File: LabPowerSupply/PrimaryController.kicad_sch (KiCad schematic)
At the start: 25 parts, among them Y1 8M

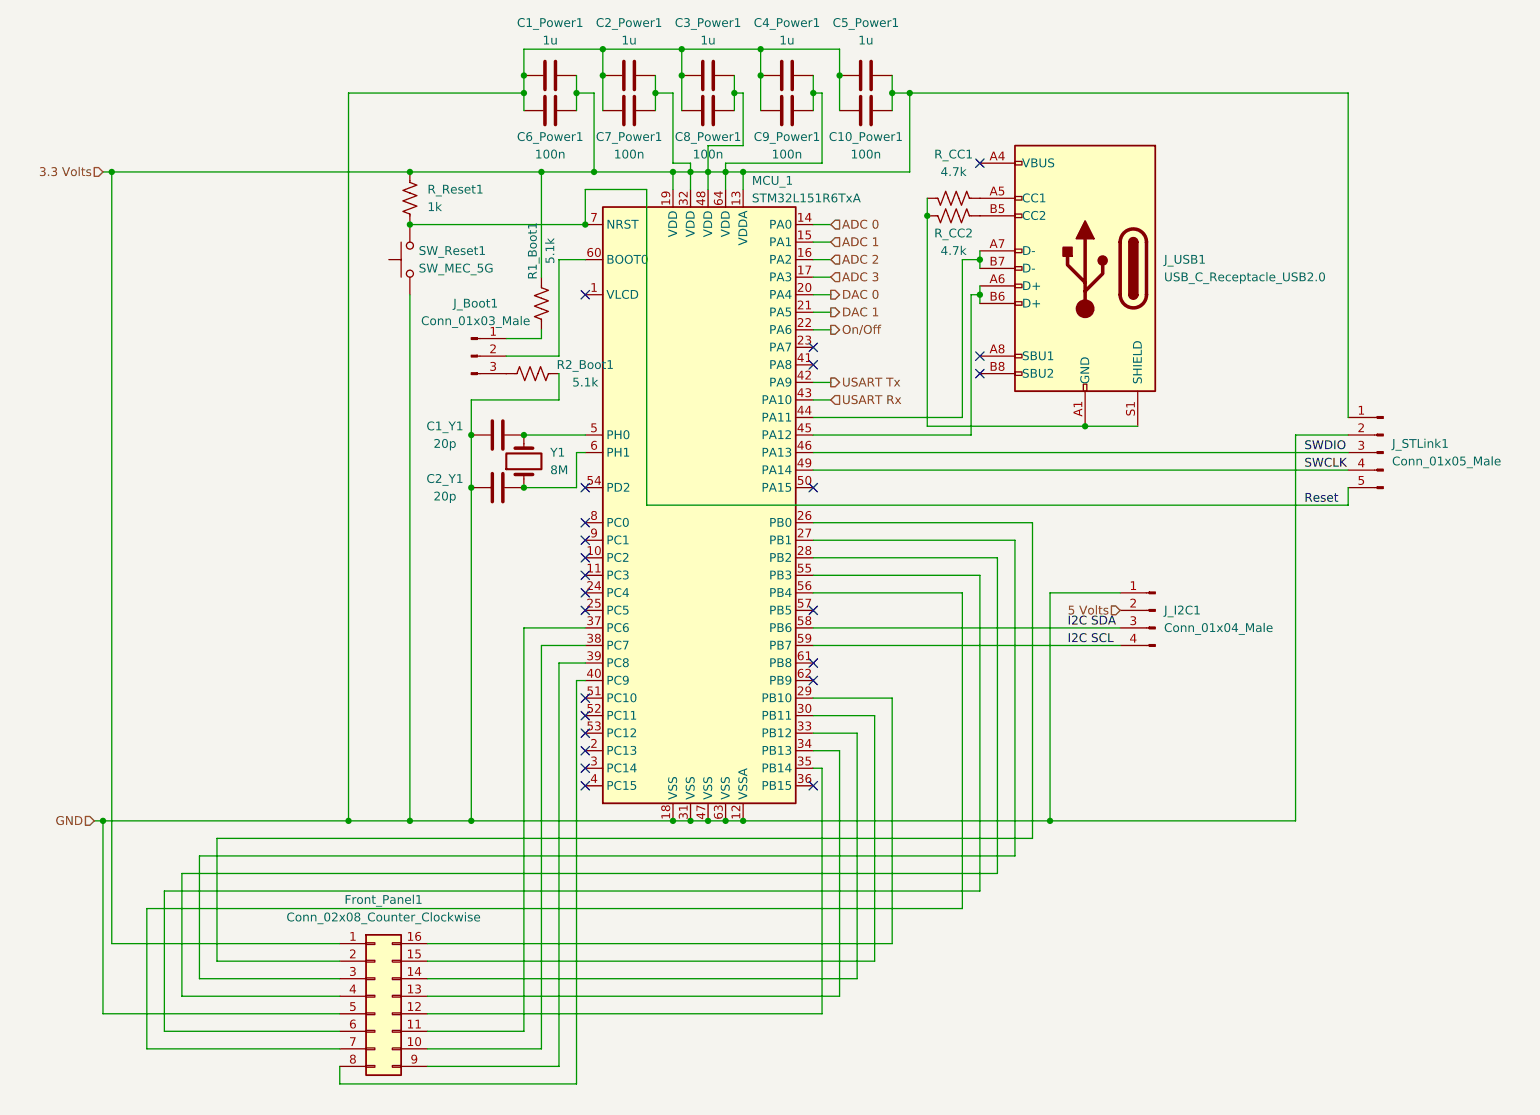
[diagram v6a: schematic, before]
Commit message: Fixed MCU communication pins and optocoupler
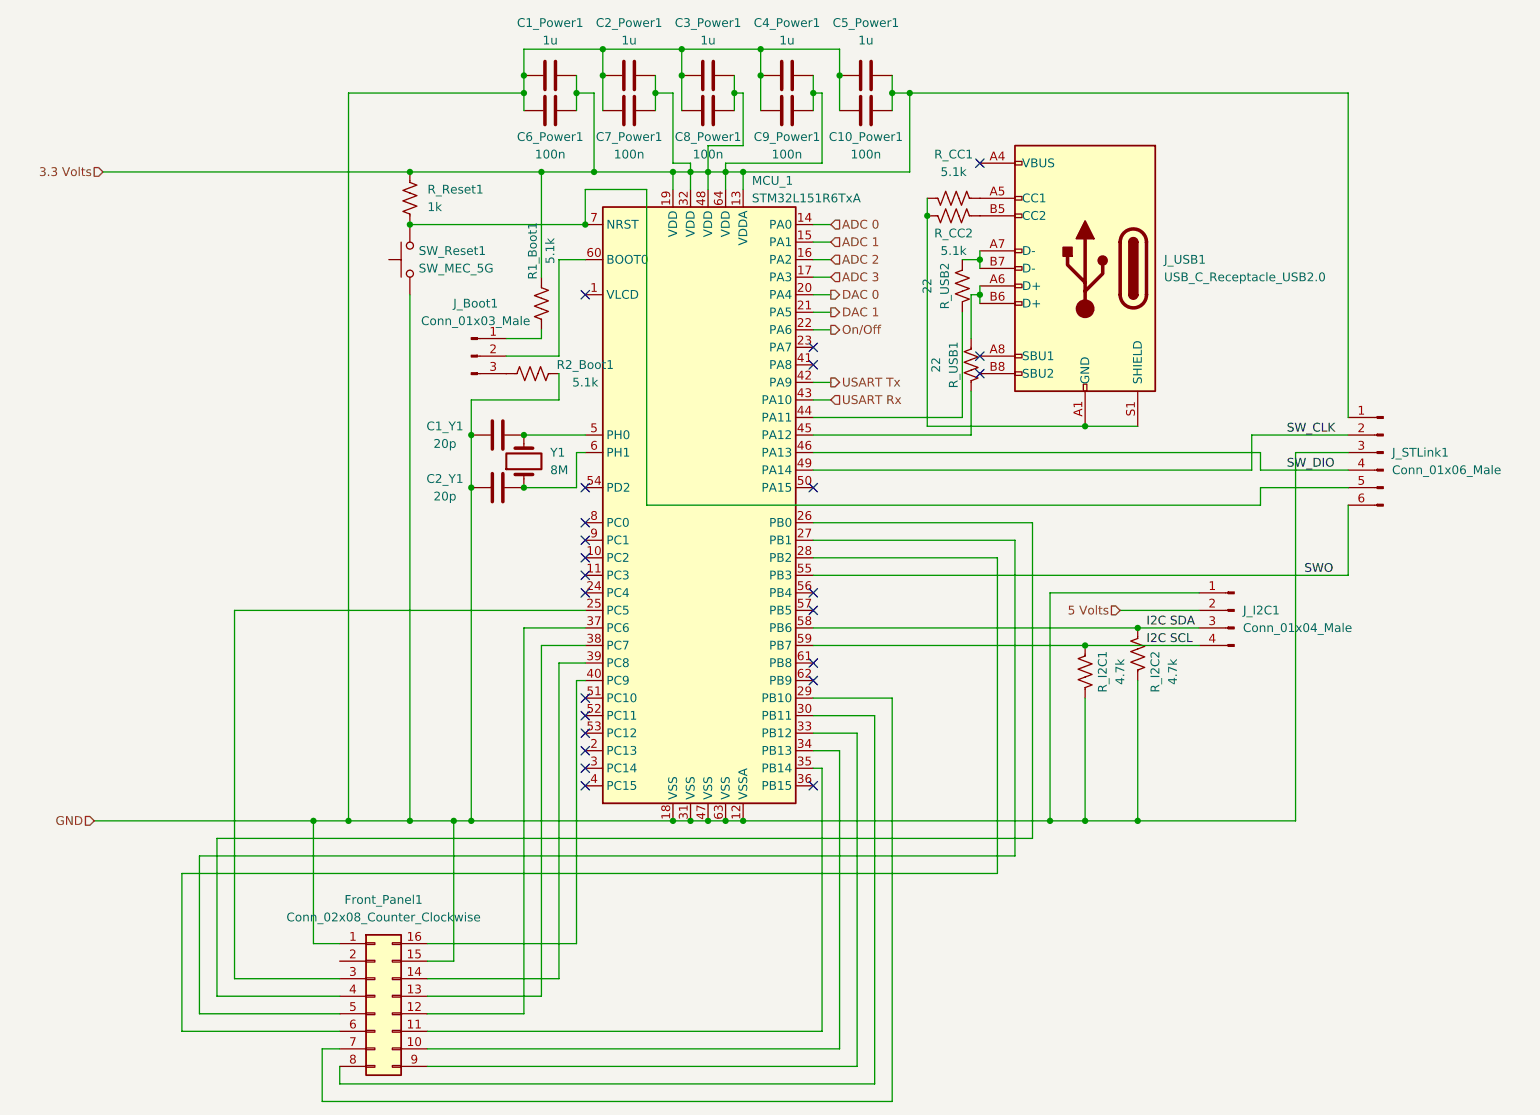
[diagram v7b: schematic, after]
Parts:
- added R_I2C1, R_I2C2: 4.7k, Resistor_SMD:R_0603_1608Metric, symbol Device:R_US
- added R_USB1, R_USB2: 22, Resistor_SMD:R_0603_1608Metric, symbol Device:R_US
- J_STLink1: value Conn_01x05_Male -> Conn_01x06_Male; footprint Connector_PinHeader_2.54mm:PinHeader_1x05_P2.54mm_Vertical -> Connector_PinHeader_2.54mm:PinHeader_1x06_P2.54mm_Vertical; symbol Connector:Conn_01x05_Male -> Connector:Conn_01x06_Male
- R_CC1, R_CC2: value 4.7k -> 5.1k
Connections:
- net 3.3 Volts: no longer Front_Panel1.1 (Pin_1)
- net GND: now also Front_Panel1.1 (Pin_1), Front_Panel1.15 (Pin_15), J_STLink1.3 (Pin_3), R_I2C1.2, R_I2C2.2; no longer Front_Panel1.5 (Pin_5), J_STLink1.2 (Pin_2)
- net I2C SCL: now also R_I2C1.1
- net I2C SDA: now also R_I2C2.1
- net at Front_Panel1.10 (Pin_10): now also MCU_1.34 (PB13); no longer MCU_1.38 (PC7)
- net at Front_Panel1.11 (Pin_11): now also MCU_1.35 (PB14); no longer MCU_1.37 (PC6)
- net at Front_Panel1.12 (Pin_12): now also MCU_1.37 (PC6); no longer MCU_1.35 (PB14)
- net at Front_Panel1.13 (Pin_13): now also MCU_1.38 (PC7); no longer MCU_1.34 (PB13)
- net at Front_Panel1.14 (Pin_14): now also MCU_1.39 (PC8); no longer MCU_1.33 (PB12)
- net at MCU_1.30 (PB11): now also Front_Panel1.8 (Pin_8); no longer Front_Panel1.15 (Pin_15)
- net at Front_Panel1.16 (Pin_16): now also MCU_1.40 (PC9); no longer MCU_1.29 (PB10)
- net at Front_Panel1.2 (Pin_2): no longer MCU_1.26 (PB0)
- net at Front_Panel1.3 (Pin_3): now also MCU_1.25 (PC5); no longer MCU_1.27 (PB1)
- net at Front_Panel1.4 (Pin_4): now also MCU_1.26 (PB0); no longer MCU_1.28 (PB2)
- net at Front_Panel1.6 (Pin_6): now also MCU_1.28 (PB2); no longer MCU_1.55 (PB3)
- net at Front_Panel1.7 (Pin_7): now also MCU_1.29 (PB10); no longer MCU_1.56 (PB4)
- net at Front_Panel1.9 (Pin_9): now also MCU_1.33 (PB12); no longer MCU_1.39 (PC8)
- net at J_USB1.A6 (D+), J_USB1.B6 (D+): now also R_USB1.2; no longer MCU_1.45 (PA12)
- net at J_USB1.A7 (D-), J_USB1.B7 (D-): now also R_USB2.2; no longer MCU_1.44 (PA11)
- net Reset: no longer names the net of J_STLink1.5 (Pin_5), MCU_1.7 (NRST), R_Reset1.2, SW_Reset1.2
- net SWCLK renamed SW_CLK
- net SW_CLK: now also J_STLink1.2 (Pin_2); no longer J_STLink1.4 (Pin_4)
- net SWDIO renamed SW_DIO
- net SW_DIO: now also J_STLink1.4 (Pin_4); no longer J_STLink1.3 (Pin_3)
- new net: MCU_1.44 (PA11), R_USB2.1
- new net: Front_Panel1.5 (Pin_5), MCU_1.27 (PB1)
- new net: MCU_1.45 (PA12), R_USB1.1
- new net SWO: J_STLink1.6 (Pin_6), MCU_1.55 (PB3)
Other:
- moved on the sheet: J_I2C1

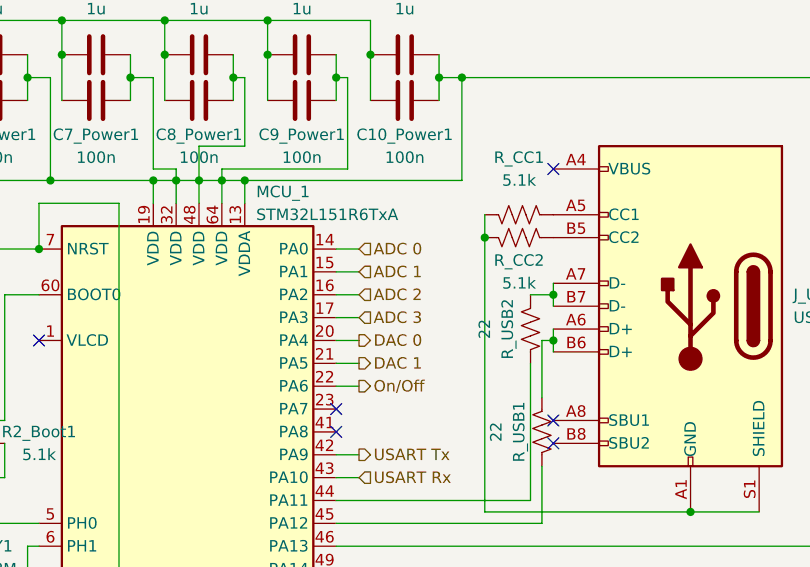
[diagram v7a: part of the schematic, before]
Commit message: Began mcu placement
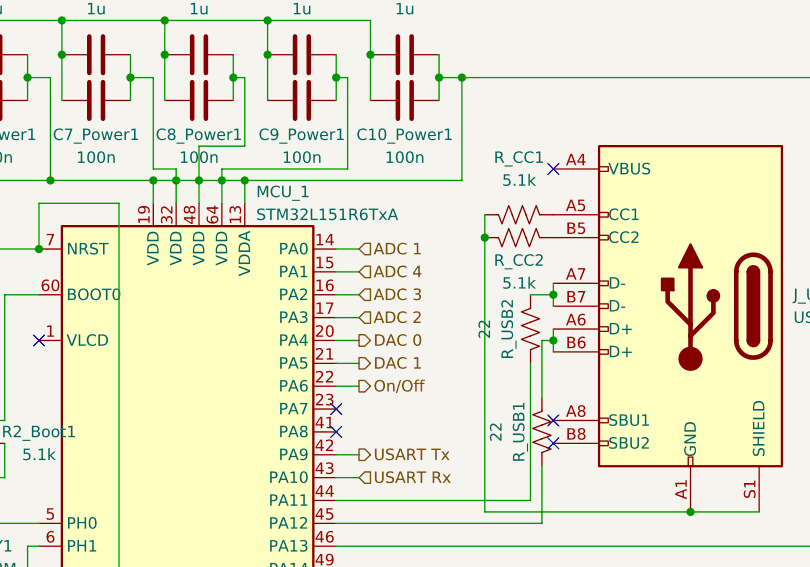
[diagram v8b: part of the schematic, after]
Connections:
- net ADC 0 is gone; now on net ADC 1: MCU_1.14 (PA0)
- net ADC 1: no longer MCU_1.15 (PA1)
- net ADC 2: now also MCU_1.17 (PA3); no longer MCU_1.16 (PA2)
- net ADC 3: now also MCU_1.16 (PA2); no longer MCU_1.17 (PA3)
- new net ADC 4: MCU_1.15 (PA1)
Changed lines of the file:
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@@
     (effects (font (size 1.27 1.27)) (justify left bottom))
   )
-  (hierarchical_label "ADC 2" (shape input) (at 138.43 49.53 0)
+  (hierarchical_label "ADC 3" (shape input) (at 138.43 49.53 0)
     (effects (font (size 1.27 1.27)) (justify left))
   )
@@
     (effects (font (size 1.27 1.27)) (justify left))
   )
-  (hierarchical_label "ADC 0" (shape input) (at 138.43 44.45 0)
+  (hierarchical_label "ADC 1" (shape input) (at 138.43 44.45 0)
     (effects (font (size 1.27 1.27)) (justify left))
   )
@@
     (effects (font (size 1.27 1.27)) (justify right))
   )
-  (hierarchical_label "ADC 3" (shape input) (at 138.43 52.07 0)
+  (hierarchical_label "ADC 2" (shape input) (at 138.43 52.07 0)
     (effects (font (size 1.27 1.27)) (justify left))
   )
-  (hierarchical_label "ADC 1" (shape input) (at 138.43 46.99 0)
+  (hierarchical_label "ADC 4" (shape input) (at 138.43 46.99 0)
     (effects (font (size 1.27 1.27)) (justify left))
   )
